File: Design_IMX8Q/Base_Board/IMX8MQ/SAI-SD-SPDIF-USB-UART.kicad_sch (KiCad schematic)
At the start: 9 parts, among them U1 MIMX8MQ6CVAHZAB, U6 SDINBDG4-8G

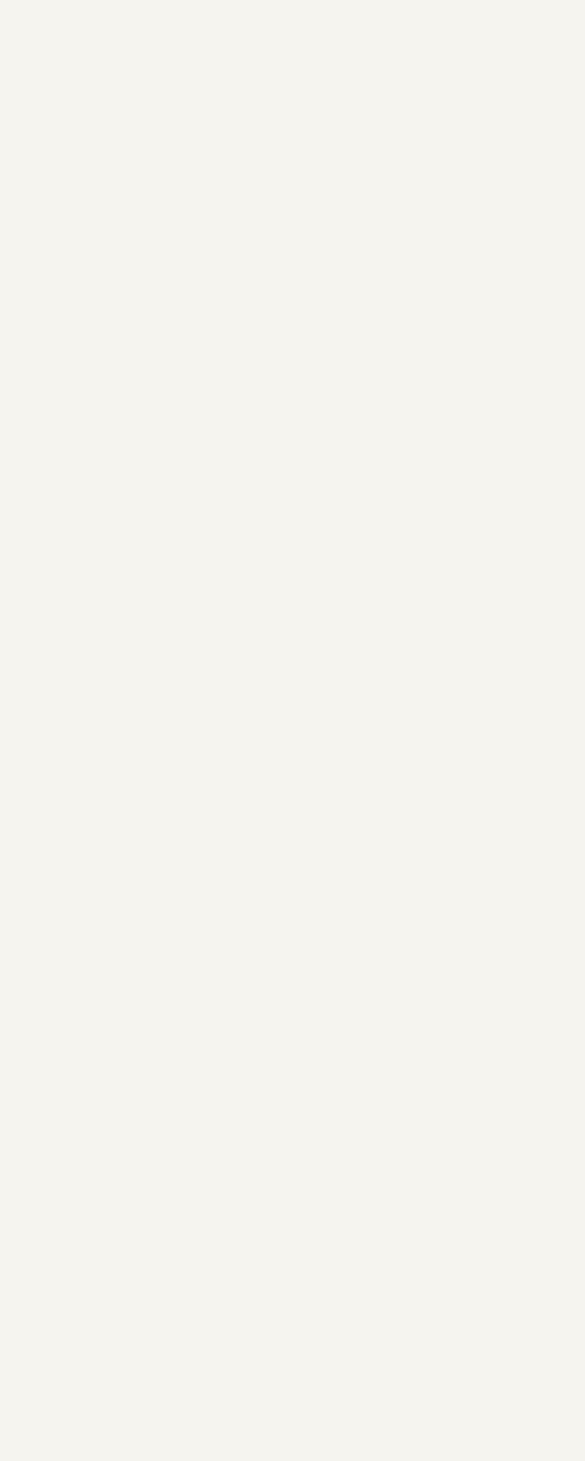
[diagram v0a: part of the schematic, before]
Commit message: Add library to WIFI/BLE
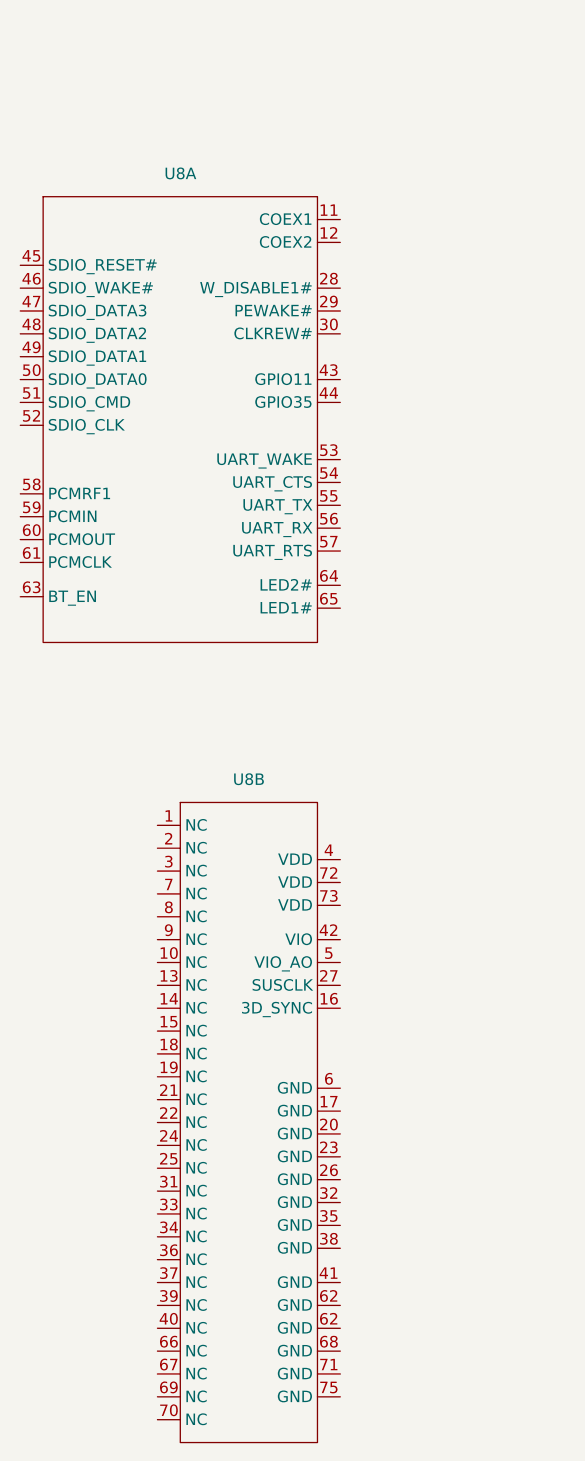
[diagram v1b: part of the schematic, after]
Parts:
- added U8: ~, _W_SBC:WG3221-00_DTS_R01, symbol _W_MX8M:WG3221
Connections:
- new net: U8.100 (GND), U8.101 (GND), U8.102 (GND), U8.103 (GND), U8.104 (GND), U8.105 (GND), U8.106 (GND), U8.107 (GND), U8.108 (GND), U8.75 (GND), U8.76 (GND), U8.77 (GND), U8.78 (GND), U8.79 (GND), U8.80 (GND), U8.81 (GND), U8.82 (GND), U8.83 (GND), U8.84 (GND), U8.85 (GND), U8.86 (GND), U8.87 (GND), U8.88 (GND), U8.89 (GND), U8.90 (GND), U8.91 (GND), U8.92 (GND), U8.93 (GND), U8.94 (GND), U8.95 (GND), U8.96 (GND), U8.97 (GND), U8.98 (GND), U8.99 (GND)

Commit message: changes vias pad size
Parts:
- added U10, U11: PCMF3USB3S, Package_CSP:Nexperia_WLCSP-15_6-3-6_2.37x1.17mm_Layout6x3_P0.4mm, symbol Power_Protection:PCMF3USB3S
- added U9: PTN36043ABXY, _W_SBC:DHX2QFN18_SOT1442-1_NXP, symbol PTN36043ABXY:PTN36043ABXY
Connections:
- net GND: now also U8.100 (GND), U8.101 (GND), U8.102 (GND), U8.103 (GND), U8.104 (GND), U8.105 (GND), U8.106 (GND), U8.107 (GND), U8.108 (GND), U8.17 (GND), U8.20 (GND), U8.23 (GND), U8.26 (GND), U8.32 (GND), U8.35 (GND), U8.38 (GND), U8.41 (GND), U8.6 (GND), U8.62 (GND), U8.68 (GND), U8.71 (GND), U8.75 (GND), U8.76 (GND), U8.77 (GND), U8.78 (GND), U8.79 (GND), U8.80 (GND), U8.81 (GND), U8.82 (GND), U8.83 (GND), U8.84 (GND), U8.85 (GND), U8.86 (GND), U8.87 (GND), U8.88 (GND), U8.89 (GND), U8.90 (GND), U8.91 (GND), U8.92 (GND), U8.93 (GND), U8.94 (GND), U8.95 (GND), U8.96 (GND), U8.97 (GND), U8.98 (GND), U8.99 (GND)
- net WIFI/BLE_SDIO_nRST: now reaches U8.45 (SDIO_RESET#)
- net WIFI/BLE_SDIO_nRST: now also U1.R22 (SD2_RESET_B)
- net WIFI/BLE_SDIO_STROBE: now reaches U8.46 (SDIO_WAKE#)
- net WIFI/BLE_SDIO_STROBE: now also U1.M21 (SD2_WP)
- net WIFI/BLE_SDIO_DATA3: now reaches U8.47 (SDIO_DATA3)
- net WIFI/BLE_SDIO_DATA3: now also U1.P21 (SD2_DATA3)
- net WIFI/BLE_SDIO_DATA2: now reaches U8.48 (SDIO_DATA2)
- net WIFI/BLE_SDIO_DATA2: now also U1.P22 (SD2_DATA2)
- net WIFI/BLE_SDIO_DATA1: now reaches U8.49 (SDIO_DATA1)
- net WIFI/BLE_SDIO_DATA1: now also U1.N21 (SD2_DATA1)
- net WIFI/BLE_SDIO_DATA0: now reaches U8.50 (SDIO_DATA0)
- net WIFI/BLE_SDIO_DATA0: now also U1.N22 (SD2_DATA0)
- net WIFI/BLE_SDIO_CMD: now reaches U8.51 (SDIO_CMD)
- net WIFI/BLE_SDIO_CMD: now also U1.M22 (SD2_CMD)
- net WIFI/BLE_SDIO_CLK: now reaches U8.52 (SDIO_CLK)
- net WIFI/BLE_SDIO_CLK: now also U1.L22 (SD2_CLK)
- net WIFI/BLE_CTS: now reaches U8.54 (UART_CTS)
- net WIFI/BLE_TX: now reaches U8.55 (UART_TX)
- net WIFI/BLE_TX: now also U1.A6 (UART3_RXD)
- net WIFI/BLE_RX: now reaches U8.56 (UART_RX)
- net WIFI/BLE_RX: now also U1.B7 (UART3_TXD)
- net WIFI/BLE_RTS: now reaches U8.57 (UART_RTS)
- net WIFI/BLE_PCMRF1: now reaches U8.58 (PCMRF1)
- net WIFI/BLE_PCMRF1: now also U1.J4 (SAI2_RXFS)
- net WIFI/BLE_SDIO_PCMIN: now reaches U8.59 (PCMIN)
- net WIFI/BLE_SDIO_PCMIN: now also U1.G5 (SAI2_TXD0)
- net WIFI/BLE_SDIO_PCMOUT: now reaches U8.60 (PCMOUT)
- net WIFI/BLE_SDIO_PCMOUT: now also U1.H6 (SAI2_RXD0)
- net WIFI/BLE_SDIO_PCMCLK: now reaches U8.61 (PCMCLK)
- net WIFI/BLE_SDIO_PCMCLK: now also U1.J5 (SAI2_TXC)
- net WIFI/BLE_SDIO_BT_EN: now reaches U8.63 (BT_EN)
- net USB1_RESREF: now reaches U1.A11 (USB1_RESREF)
- net USB1_RX_P: now reaches U1.A12 (USB1_RX_P)
- net USB1_RX_P: now also U9.18 (RX_AP_+)
- net USB1_TX_P: now reaches U1.A13 (USB1_TX_P)
- net USB1_TX_P: now also U9.15 (TX_AP_)
- net USB1_DP: now reaches U1.A14 (USB1_DP)
- net USB1_DP: now also U10.C5 (CH3_OUT+)
- net USB1_RX_N: now reaches U1.B12 (USB1_RX_N)
- net USB1_RX_N: now also U9.17 (RX_AP_)
- net USB1_TX_N: now reaches U1.B13 (USB1_TX_N)
- net USB1_TX_N: now also U9.14 (TX_AP_)
- net USB1_DN: now reaches U1.B14 (USB1_DN)
- net USB1_DN: now also U10.C6 (CH3_OUT-)
- net USB1_ID: now reaches U1.C14 (USB1_ID)
- net USB1_VBUS: now reaches U1.D14 (USB1_VBUS)
- net at U8.4 (VDD): now also U8.72 (VDD), U8.73 (VDD)
- new net: U11.C3 (CH2_OUT+), U9.9 (RX_CON_2+)
- new net: U11.C4 (CH2_OUT-), U9.8 (RX_CON_2-)
- new net: U11.C1 (CH1_OUT+), U9.2 (RX_CON_1+)
- new net: U11.C2 (CH1_OUT-), U9.3 (RX_CON_1-)
- new net: U10.C1 (CH1_OUT+), U9.12 (TX_CON_2+)
- new net: U10.C2 (CH1_OUT-), U9.11 (TX_CON_2-)
- new net: U10.C3 (CH2_OUT+), U9.7 (TX_CON_1-)
- new net: U10.C4 (CH2_OUT-), U9.6 (TX_CON_1+)
- no-connect marks 0 -> 27
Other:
- moved on the sheet: C24, C25, C26, C27, C28, C29, C30, U1E, U6, U8A, U8B

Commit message: Add QSPI and more color
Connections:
- net UART1_TXD: now reaches U1.A7 (UART1_TXD)
- net SAI1_TXD2: now reaches U1.B2 (SAI1_TXD2)
- net SAI1_TXD6: now reaches U1.B3 (SAI1_TXD6)
- net UART2_RXD: now reaches U1.B6 (UART2_RXD)
- net SAI1_TXD7: now reaches U1.C1 (SAI1_TXD7)
- net SAI1_TXD5: now reaches U1.C2 (SAI1_TXD5)
- net SAI3_TXD: now reaches U1.C3 (SAI3_TXD)
- net SAI3_TXC: now reaches U1.C4 (SAI3_TXC)
- net UART2_CTS_B: now reaches U1.C6 (UART4_RXD)
- net UART1_RXD: now reaches U1.C7 (UART1_RXD)
- net SAI1_TXD3: now reaches U1.D1 (SAI1_TXD3)
- net SAI1_TXD4: now reaches U1.D2 (SAI1_TXD4)
- net SAI3_MCLK: now reaches U1.D3 (SAI3_MCLK)
- net UART2_TXD: now reaches U1.D6 (UART2_TXD)
- net UART2_RTS_B: now reaches U1.D7 (UART4_TXD)
- net SAI1_TXD1: now reaches U1.E2 (SAI1_TXD1)
- net SAI1_RXD5: now reaches U1.F1 (SAI1_RXD5)
- net SAI1_TXD0: now reaches U1.F2 (SAI1_TXD0)
- net SAI3_RXD: now reaches U1.F3 (SAI3_RXD)
- net SAI3_RXC: now reaches U1.F4 (SAI3_RXC)
- net SAI1_RXD7: now reaches U1.G1 (SAI1_RXD7)
- net SAI1_RXD6: now reaches U1.G2 (SAI1_RXD6)
- net SAI3_TXFS: now reaches U1.G3 (SAI3_TXFS)
- net SAI3_RXFS: now reaches U1.G4 (SAI3_RXFS)
- net SAI1_RXD2: now reaches U1.H2 (SAI1_RXD2)
- net SAI1_RXD4: now reaches U1.J1 (SAI1_RXD4)
- net SAI1_RXD3: now reaches U1.J2 (SAI1_RXD3)
- net SAI1_RXD0: now reaches U1.K2 (SAI1_RXD0)
- net SAI1_RXD1: now reaches U1.L2 (SAI1_RXD1)

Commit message: it was inserted power control system
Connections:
- net SAI2_MCLK: now also U1.H5 (SAI2_MCLK)
- net SAI2_RXC: now also U1.H3 (SAI2_RXC)
- net SAI2_TXFS: now also U1.H4 (SAI2_TXFS)
- net VDD_3V3: now also U8.4 (VDD), U8.72 (VDD), U8.73 (VDD)
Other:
- moved on the sheet: U1E
